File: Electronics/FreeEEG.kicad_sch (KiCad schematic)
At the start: 121 parts, among them J1 ConnElectrodes, J2 10137065-00021LF, Q1 2N7002, Q2 2N7002, Q3 2N7002, SW1 ON_SW, SW2 SEL_SW, SW3 RST_BTN, SW4 BOOT_BTN, U1 ADS1299, U2 OPA376xxDBV, U3 ESP32-S3-WROOM-1, U4 OPA376xxDBV, U5 XL1509-3.3, U6 NCP1117-5.0_SOT223, U7 MPU-6050

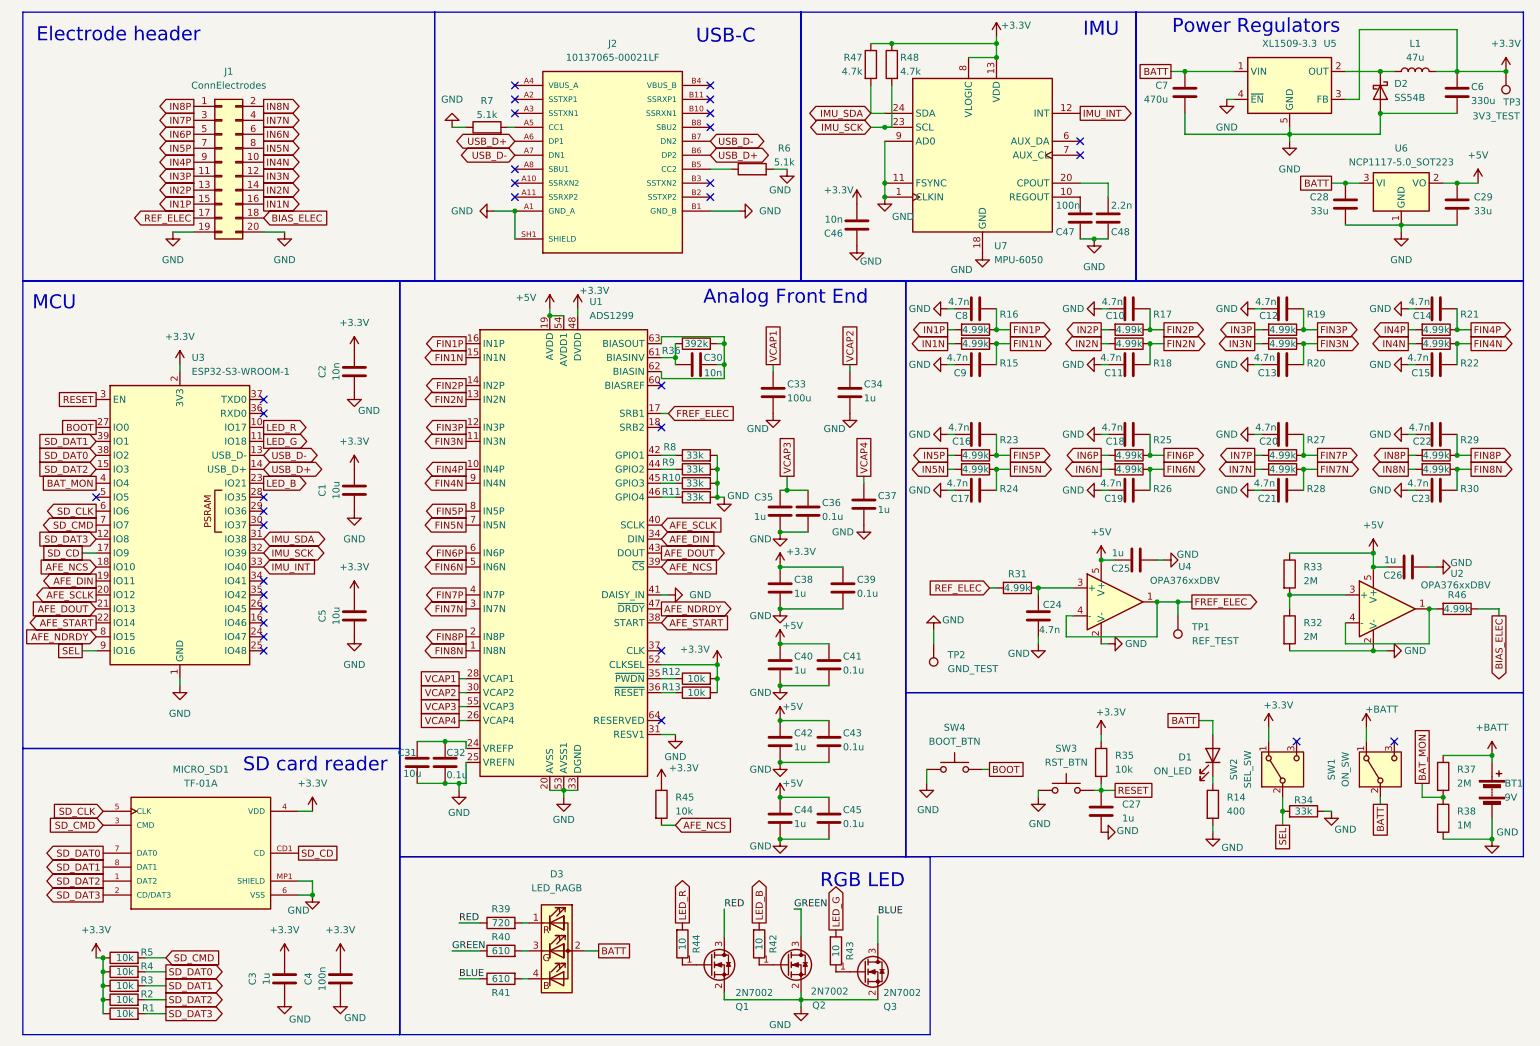
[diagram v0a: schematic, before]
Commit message: New board release and adding support for ws2812 LED
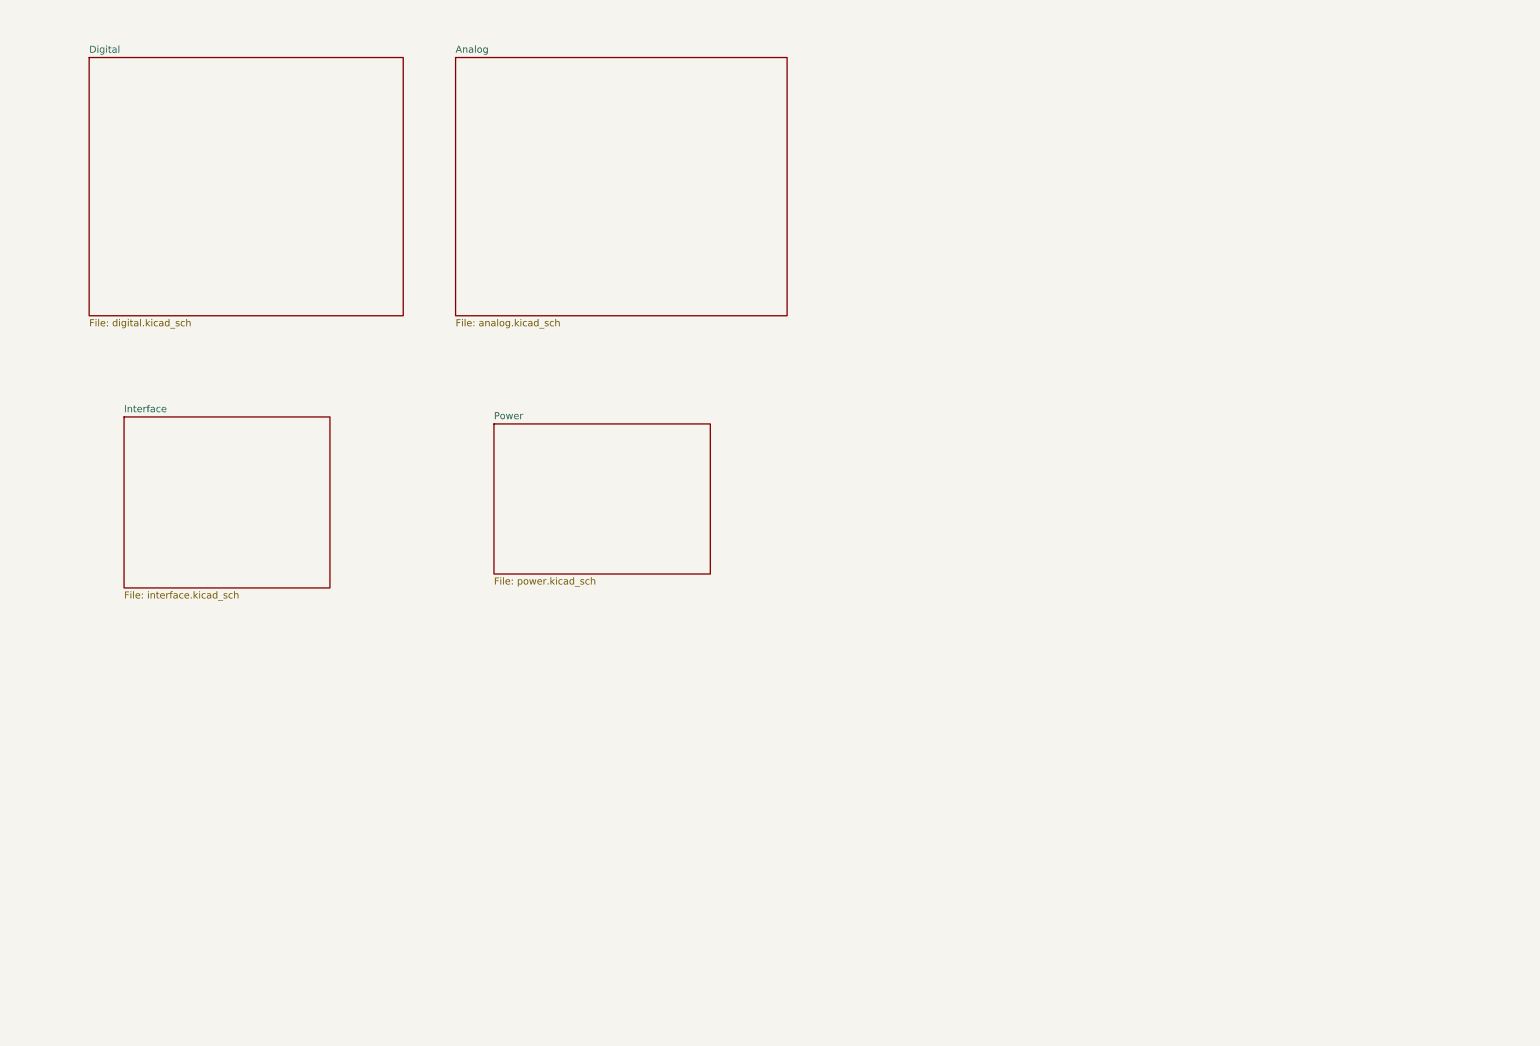
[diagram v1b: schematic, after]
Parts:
- removed BT1: 9V, Connector_PinHeader_2.54mm:PinHeader_1x02_P2.54mm_Vertical, symbol Device:Battery
- removed C1, C31, C5: 10u, Capacitor_SMD:C_0805_2012Metric, symbol Device:C
- removed C10, C11, C12, C13, C14, C15, C16, C17, C18, C19, C20, C21, C22, C23, C24, C8, C9: 4.7n, Capacitor_SMD:C_0603_1608Metric, symbol Device:C
- removed C2: 10n, Capacitor_SMD:C_0805_2012Metric, symbol Device:C
- removed C25, C26, C27, C3: 1u, Capacitor_SMD:C_0805_2012Metric, symbol Device:C
- removed C28, C29: 33u, Capacitor_SMD:C_1206_3216Metric, symbol Device:C
- removed C30, C46: 10n, Capacitor_SMD:C_0603_1608Metric, symbol Device:C
- removed C32, C36, C39, C41, C43, C45: 0.1u, Capacitor_SMD:C_0603_1608Metric, symbol Device:C
- removed C33: 100u, Capacitor_SMD:C_Elec_6.3x7.7, symbol Device:C
- removed C34, C35, C37, C38, C40, C42, C44: 1u, Capacitor_SMD:C_0603_1608Metric, symbol Device:C
- removed C4: 100n, Capacitor_SMD:C_0805_2012Metric, symbol Device:C
- removed C47: 100n, Capacitor_SMD:C_0603_1608Metric, symbol Device:C
- removed C48: 2.2n, Capacitor_SMD:C_0603_1608Metric, symbol Device:C
- removed C6: 330u, Capacitor_SMD:C_Elec_8x10.2, symbol Device:C
- removed C7: 470u, Capacitor_SMD:C_Elec_8x10.2, symbol Device:C
- removed D1: ON_LED, LED_SMD:LED_0805_2012Metric, symbol Device:LED
- removed D2: SS54B, Diode_SMD:D_SMB, symbol Device:D_Schottky
- removed D3: LED_RAGB, XL-3528RGBW-HM:XL-3528RGBW-HM, symbol Device:LED_RAGB
- removed J1: ConnElectrodes, Connector_PinHeader_2.54mm:PinHeader_2x10_P2.54mm_Vertical, symbol Connector_Generic:Conn_02x10_Odd_Even
- removed J2: 10137065-00021LF, 10137065-00021LF:AMPHENOL_10137065-00021LF, symbol 10137065-00021LF:10137065-00021LF
- removed L1: 47u, Inductor_SMD:L_Bourns_SRP7028A_7.3x6.6mm, symbol Device:L
- removed MICRO_SD1: TF-01A, TF-01A:TF-01A, symbol TF-01A:TF-01A
- removed Q1, Q2, Q3: 2N7002, Package_TO_SOT_SMD:SOT-23, symbol Transistor_FET:2N7002
- removed R1, R12, R13, R2, R3, R35, R4, R45, R5: 10k, Resistor_SMD:R_0603_1608Metric, symbol Device:R
- removed R10, R11, R34, R8, R9: 33k, Resistor_SMD:R_0603_1608Metric, symbol Device:R
- removed R14: 400, Resistor_SMD:R_0805_2012Metric, symbol Device:R
- removed R15, R16, R17, R18, R19, R20, R21, R22, R23, R24, R25, R26, R27, R28, R29, R30, R31, R46: 4.99k, Resistor_SMD:R_0603_1608Metric, symbol Device:R
- removed R32, R33, R37: 2M, Resistor_SMD:R_0603_1608Metric, symbol Device:R
- removed R36: 392k, Resistor_SMD:R_0603_1608Metric, symbol Device:R
- removed R38: 1M, Resistor_SMD:R_0603_1608Metric, symbol Device:R
- removed R39: 720, Resistor_SMD:R_0805_2012Metric, symbol Device:R
- removed R40, R41: 610, Resistor_SMD:R_0805_2012Metric, symbol Device:R
- removed R42, R43, R44: 10, Resistor_SMD:R_0603_1608Metric, symbol Device:R
- removed R47, R48: 4.7k, symbol Device:R
- removed R6, R7: 5.1k, Resistor_SMD:R_0603_1608Metric, symbol Device:R
- removed SW1: ON_SW, K3-1260D-L1:K3-1260D-L1, symbol Switch:SW_SPDT
- removed SW2: SEL_SW, K3-1260D-L1:K3-1260D-L1, symbol Switch:SW_SPDT
- removed SW3: RST_BTN, K2-1187SQ-A4SW-06:K2-1187SQ-A4SW-06, symbol Switch:SW_Push
- removed SW4: BOOT_BTN, K2-1187SQ-A4SW-06:K2-1187SQ-A4SW-06, symbol Switch:SW_Push
- removed TP1: REF_TEST, TestPoint:TestPoint_Pad_D1.5mm, symbol Connector:TestPoint
- removed TP2: GND_TEST, TestPoint:TestPoint_Pad_D1.5mm, symbol Connector:TestPoint
- removed TP3: 3V3_TEST, TestPoint:TestPoint_Pad_D1.5mm, symbol Connector:TestPoint
- removed U1: ADS1299, Package_QFP:TQFP-64_10x10mm_P0.5mm, symbol Analog_ADC:ADS1299
- removed U2, U4: OPA376xxDBV, Package_TO_SOT_SMD:SOT-23-5, symbol Amplifier_Operational:OPA376xxDBV
- removed U3: ESP32-S3-WROOM-1, RF_Module:ESP32-S3-WROOM-1, symbol RF_Module:ESP32-S3-WROOM-1
- removed U5: XL1509-3.3, Package_SO:SOIC-8_3.9x4.9mm_P1.27mm, symbol Regulator_Switching:XL1509-3.3
- removed U6: NCP1117-5.0_SOT223, Package_TO_SOT_SMD:SOT-223-3_TabPin2, symbol Regulator_Linear:NCP1117-5.0_SOT223
- removed U7: MPU-6050, Sensor_Motion:InvenSense_QFN-24_4x4mm_P0.5mm, symbol Sensor_Motion:MPU-6050
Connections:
- no-connect marks 32 -> 0
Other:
- added sheet Analog (analog.kicad_sch)
- added sheet Digital (digital.kicad_sch)
- added sheet Interface (interface.kicad_sch)
- added sheet Power (power.kicad_sch)
- note removed: "Analog Front End"
- note removed: "Electrode header"
- note removed: "IMU"
- note removed: "MCU"
- note removed: "Power Regulators"
- note removed: "RGB LED"
- note removed: "SD card reader"
- note removed: "USB-C"
